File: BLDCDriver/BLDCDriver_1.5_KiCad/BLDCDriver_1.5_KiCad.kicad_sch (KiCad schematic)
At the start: 47 parts, among them IC1 STSPIN32G4, J1 Conn_01x02_Male, J2 Conn_01x07_Pin, J2 Motor Out, J4 POWER, J5 CAN, U3 MCP2562-E-SN, U5 AS5048A-HTSP-500, Y3 12Mhz

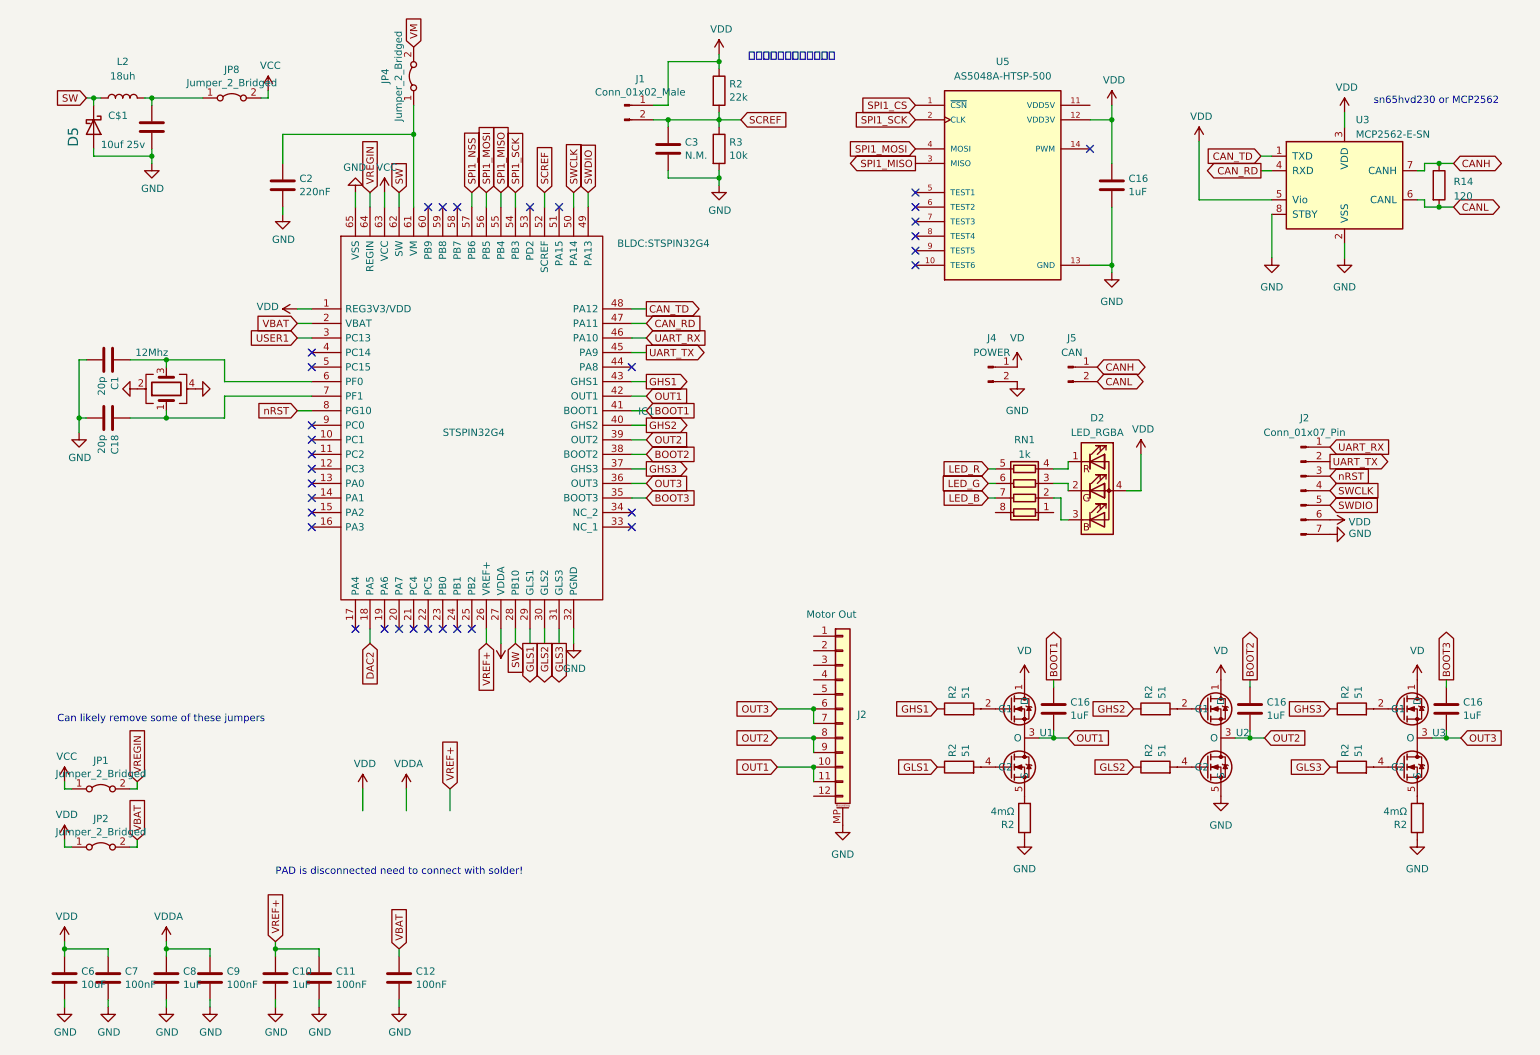
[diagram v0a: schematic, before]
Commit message: ✨回路を進めたよ。あとアートワーク太くするだけ。
CANの電源が3.3Vだと厳しい印象。
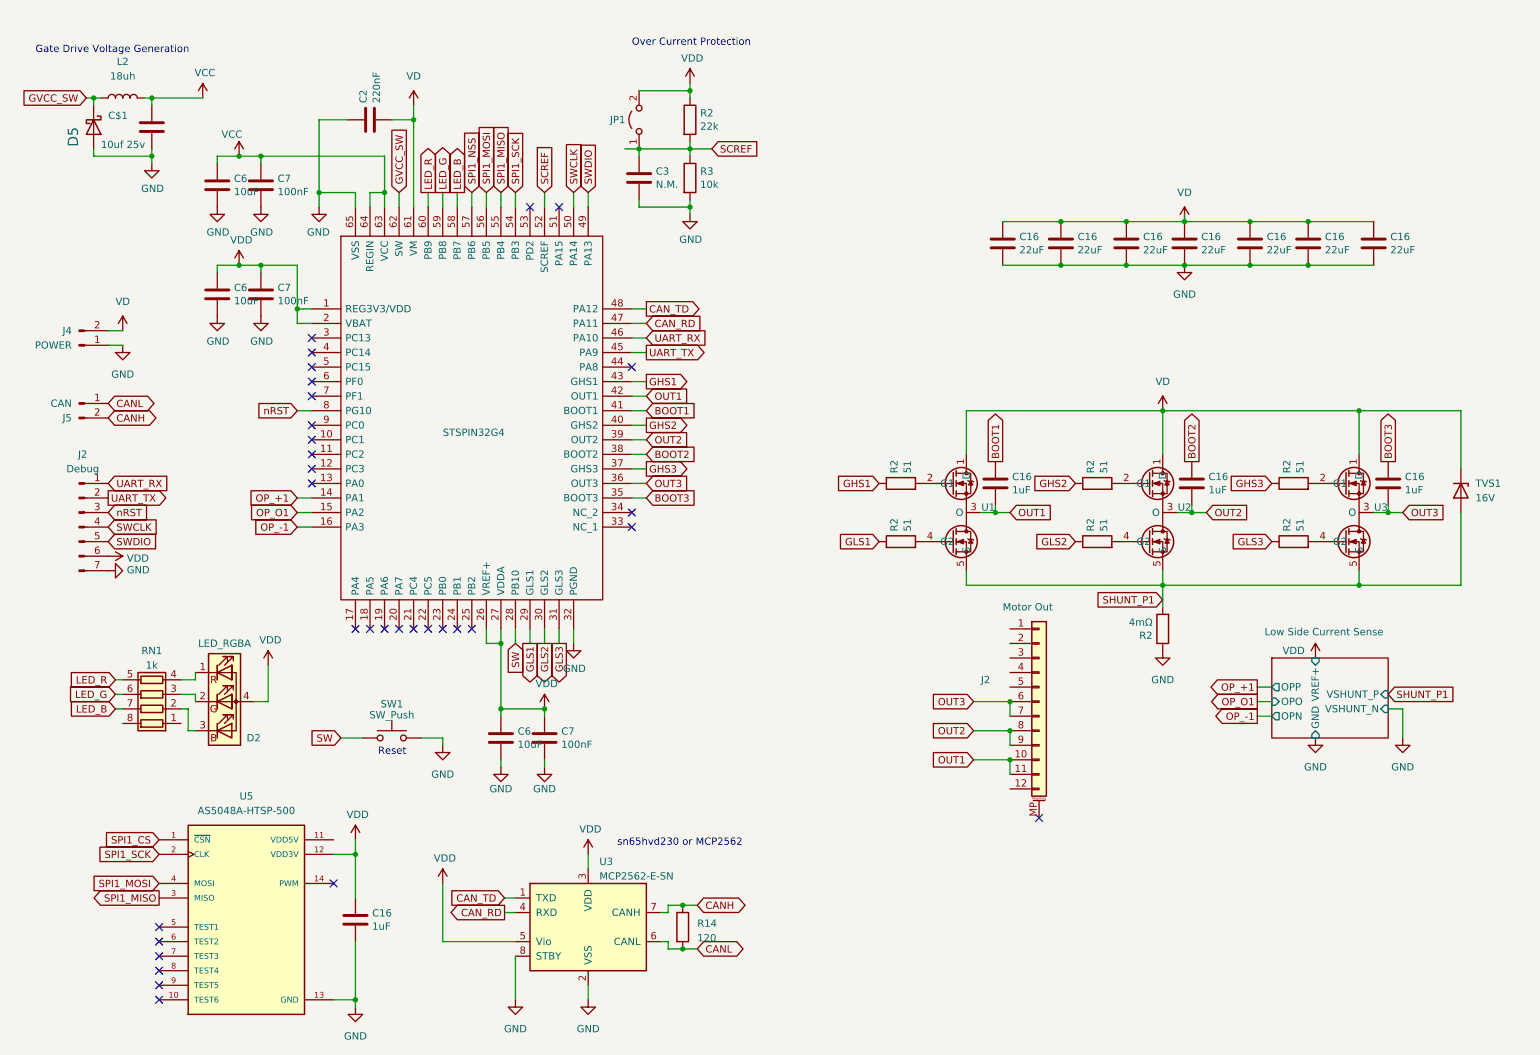
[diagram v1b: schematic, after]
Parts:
- removed C1, C18: 20p, Capacitor_SMD:C_0402_1005Metric, symbol Device:C
- removed C10, C8: 1uF, Capacitor_SMD:C_0603_1608Metric, symbol Device:C
- removed C11, C12, C7, C9: 100nF, Capacitor_SMD:C_0603_1608Metric, symbol Device:C
- removed C6: 10uF, Capacitor_SMD:C_0805_2012Metric, symbol Device:C
- removed J1: Conn_01x02_Male, Connector_PinSocket_2.54mm:PinSocket_1x02_P2.54mm_Vertical, symbol Connector:Conn_01x02_Male
- removed JP1, JP2, JP4, JP8: Jumper_2_Bridged, Jumper:SolderJumper-2_P1.3mm_Bridged_RoundedPad1.0x1.5mm, symbol Jumper:Jumper_2_Bridged
- removed R2 (x2): 4mΩ, Resistor_SMD:R_2512_6332Metric, symbol Device:R
- removed Y3: 12Mhz, Crystal:Crystal_SMD_3225-4Pin_3.2x2.5mm, symbol Device:Crystal_GND24
- added C16 (x7): 22uF, Capacitor_SMD:C_0805_2012Metric, symbol Device:C
- added C6 (x3): 10uF, Capacitor_SMD:C_0402_1005Metric, symbol Device:C
- added C7 (x3): 100nF, Capacitor_SMD:C_0402_1005Metric, symbol Device:C
- added JP1: Jumper_2_Open, Jumper:SolderJumper-2_P1.3mm_Open_RoundedPad1.0x1.5mm, symbol Jumper:Jumper_2_Open
- added R2: 4mΩ, Resistor_SMD:R_2512_6332Metric, symbol Device:R
- added SW1: SW_Push, newinov-kicad:SKRPACE010, symbol Switch:SW_Push
- added TVS1: 16V, Diode_SMD:D_SMB, symbol Device:D_Zener
- J2: value Conn_01x07_Pin -> Debug
- R14: footprint Resistor_SMD:R_0402_1005Metric_Pad0.72x0.64mm_HandSolder -> Resistor_SMD:R_0603_1608Metric_Pad0.98x0.95mm_HandSolder
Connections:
- net VBAT is gone; now on net VDD: IC1.2 (VBAT)
- net VDDA is gone; now on net VDD: IC1.27 (VDDA)
- net VREF+ is gone; now on net VDD: IC1.26 (VREF+)
- net VREGIN is gone; now on net VCC: IC1.64 (REGIN)
- net CANH: now also J5.2 (Pin_2); no longer J5.1 (Pin_1)
- net CANL: now also J5.1 (Pin_1); no longer J5.2 (Pin_2)
- net GND: now also C2.1, J4.1 (Pin_1), C16.1, C16.1, C16.1, C16.1, C16.1, C16.1, C16.1, C6.2, C6.2, C6.2, C7.2, C7.2, C7.2, R2.1, SW1.1; no longer C2.2, J2.MP (MountPin), J4.2 (Pin_2), U2.5 (S)
- net LED_B: now also IC1.58 (PB7)
- net LED_G: now also IC1.59 (PB8)
- net LED_R: now also IC1.60 (PB9)
- net SCREF: now also JP1.1 (A)
- net SW: now also SW1.2; no longer D5.1 (K), IC1.62 (SW), L2.1
- net VCC: now also C$1.1, L2.2, C6.1, C7.1
- net VD: now also C2.2, IC1.61 (VM), J4.2 (Pin_2), C16.2, C16.2, C16.2, C16.2, C16.2, C16.2, C16.2, TVS1.1 (K); no longer J4.1 (Pin_1)
- net VDD: now also C6.1, C6.1, C7.1, C7.1, JP1.2 (B)
- net SHUNT_P1: now reaches U3.5 (S)
- net SHUNT_P1: now also U1.5 (S), U2.5 (S), R2.2, TVS1.2 (A)
- net OP_+1: now reaches IC1.14 (PA1)
- net OP_O1: now reaches IC1.15 (PA2)
- net OP_-1: now reaches IC1.16 (PA3)
- net DAC2: no longer names the net of IC1.18 (PA5)
- net USER1: no longer names the net of IC1.3 (PC13)
- new net GVCC_SW: D5.1 (K), IC1.62 (SW), L2.1
- no-connect marks 33 -> 32
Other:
- added sheet Low Side Current Sense (CurrentSense.kicad_sch)
- note added: "Gate Drive Voltage Generation"
- note added: "Over Current Protection"
- note added: "Reset"
- note removed: "Can likely remove some of these jumpers"
- note removed: "PAD is disconnected need to connect with solder!"
- note removed: "入力電圧によって決定する"
- moved on the sheet: C16, C2, C3, D2, J2, J4, J5, R14, R2, R3, RN1, U1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

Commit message: ✨パワーラインのアートワークを仕上げた
[-] GNDビア
[-] CAN用LDO
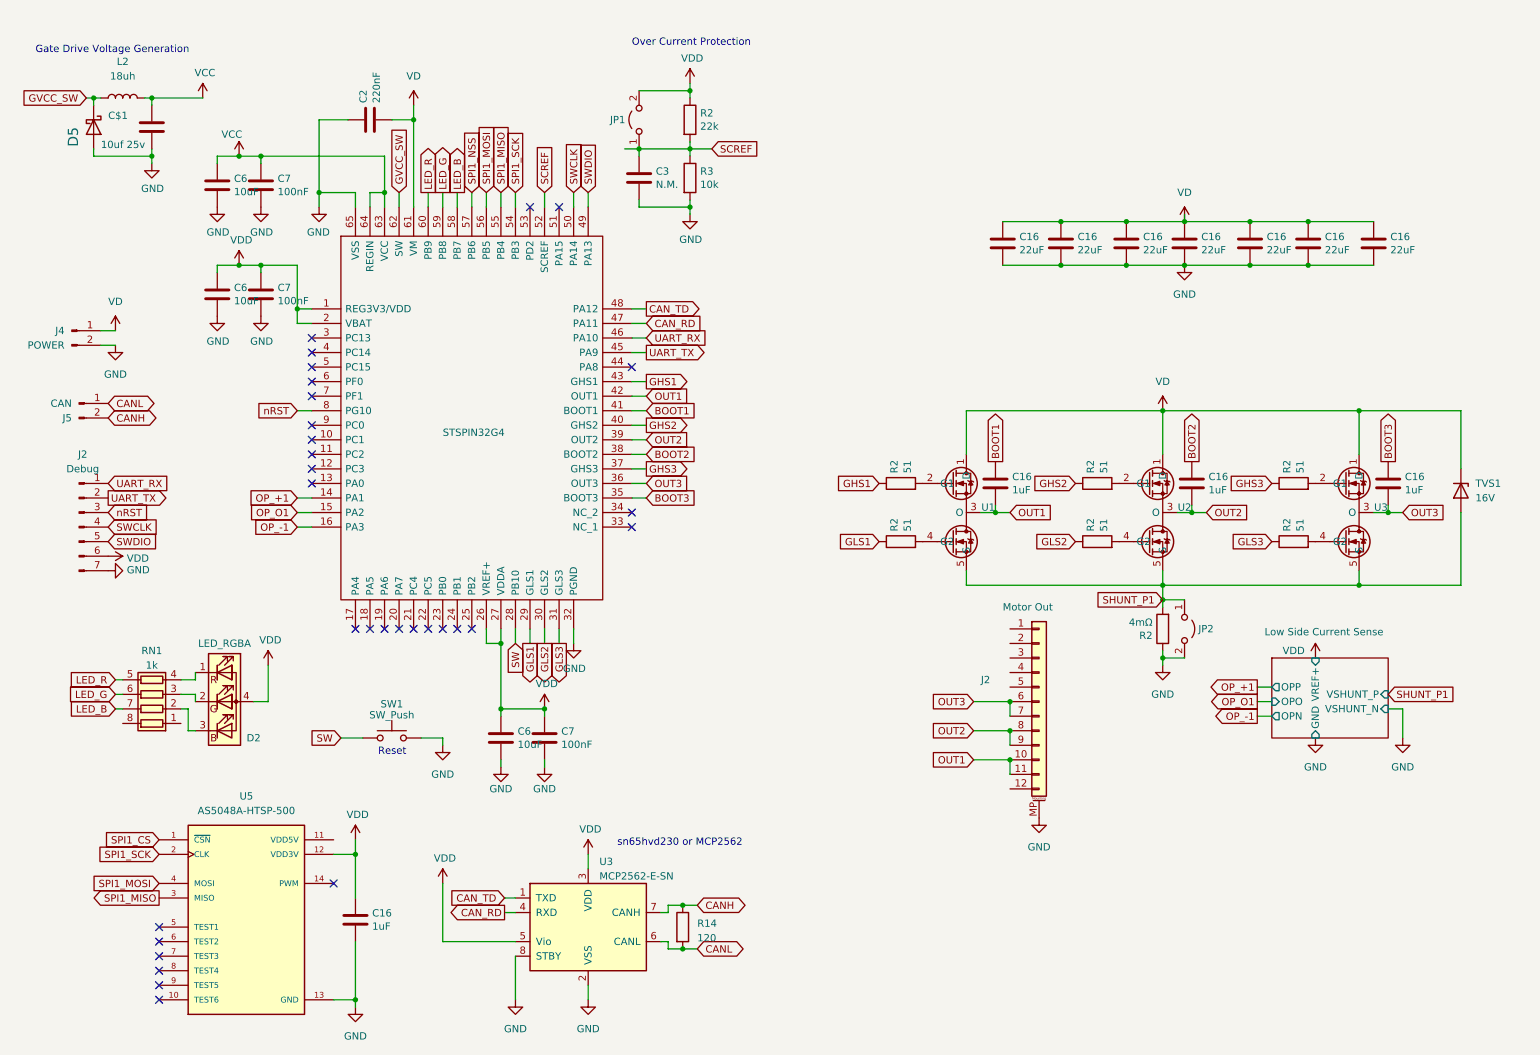
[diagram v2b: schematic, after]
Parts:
- added JP2: Jumper_2_Open, Jumper:SolderJumper-2_P1.3mm_Open_RoundedPad1.0x1.5mm, symbol Jumper:Jumper_2_Open
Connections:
- net GND: now also J2.MP (MountPin), J4.2 (Pin_2), JP2.2 (B); no longer J4.1 (Pin_1)
- net SHUNT_P1: now also JP2.1 (A)
- net VD: now also J4.1 (Pin_1); no longer J4.2 (Pin_2)
- no-connect marks 32 -> 31
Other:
- moved on the sheet: J4

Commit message: ✨ LED、LDO、ビアをやった
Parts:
- added C7 (x3): 100nF, Capacitor_SMD:C_0402_1005Metric, symbol Device:C
- added D3, D4, D5: LED, LED_SMD:LED_0603_1608Metric_Pad1.05x0.95mm_HandSolder, symbol Device:LED
- added R3 (x2): 1k, Resistor_SMD:R_0402_1005Metric, symbol Device:R
- added R3: 10k, Resistor_SMD:R_0402_1005Metric, symbol Device:R
- added U6: AP7375-33SA-7, AP7375-33SA-7_DIO, symbol BLDC_sym:AP7375-33SA-7
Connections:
- net GND: now also C7.2, C7.2, C7.2, D3.1 (K), D4.1 (K), D5.1 (K), U6.3 (GND)
- net VCC: now also C7.1, U6.1 (VIN)
- net VD: now also R3.1
- net VDD: now also R3.1; no longer U3.3 (VDD)
- net LED_Alive: now reaches IC1.53 (PD2)
- net LED_Alive: now also R3.1
- new net: D4.2 (A), R3.2
- new net: D3.2 (A), R3.2
- new net: D5.2 (A), R3.2
- new net +5V: C7.1, C7.1, U3.3 (VDD), U6.2 (VOUT)
- no-connect marks 31 -> 30

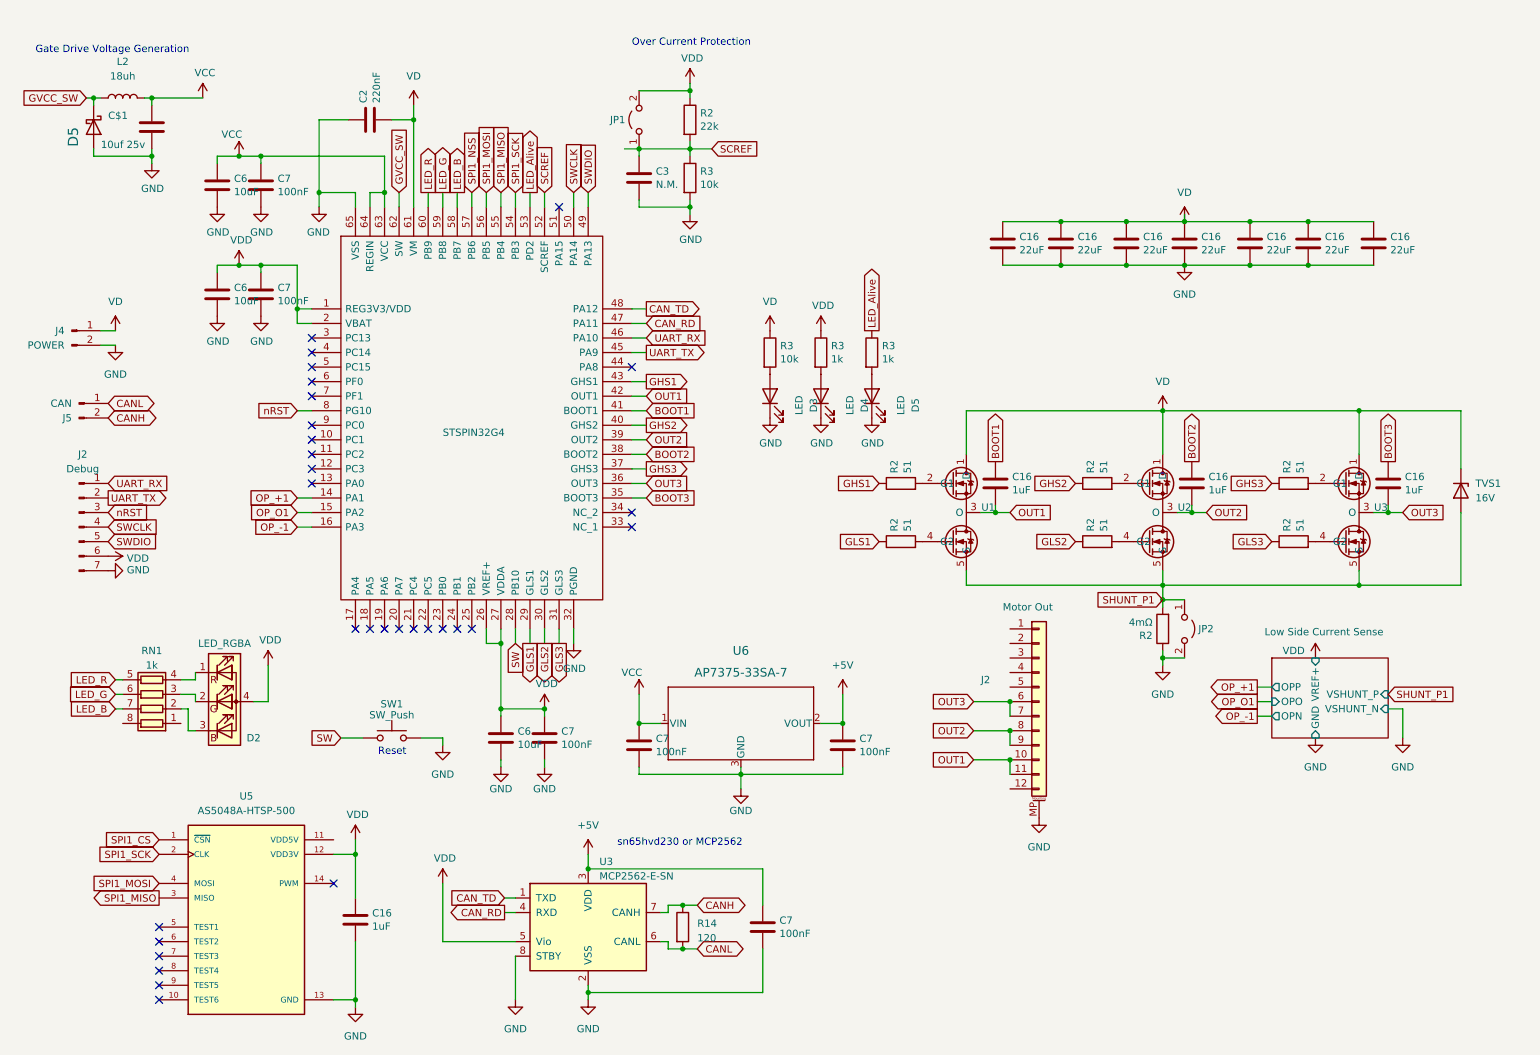
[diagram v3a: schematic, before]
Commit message: ✨ID切り替えパッド、GNDベタ、パターン禁止エリア設定、テストポイント
次は抵抗値の決定などをしていきたい。
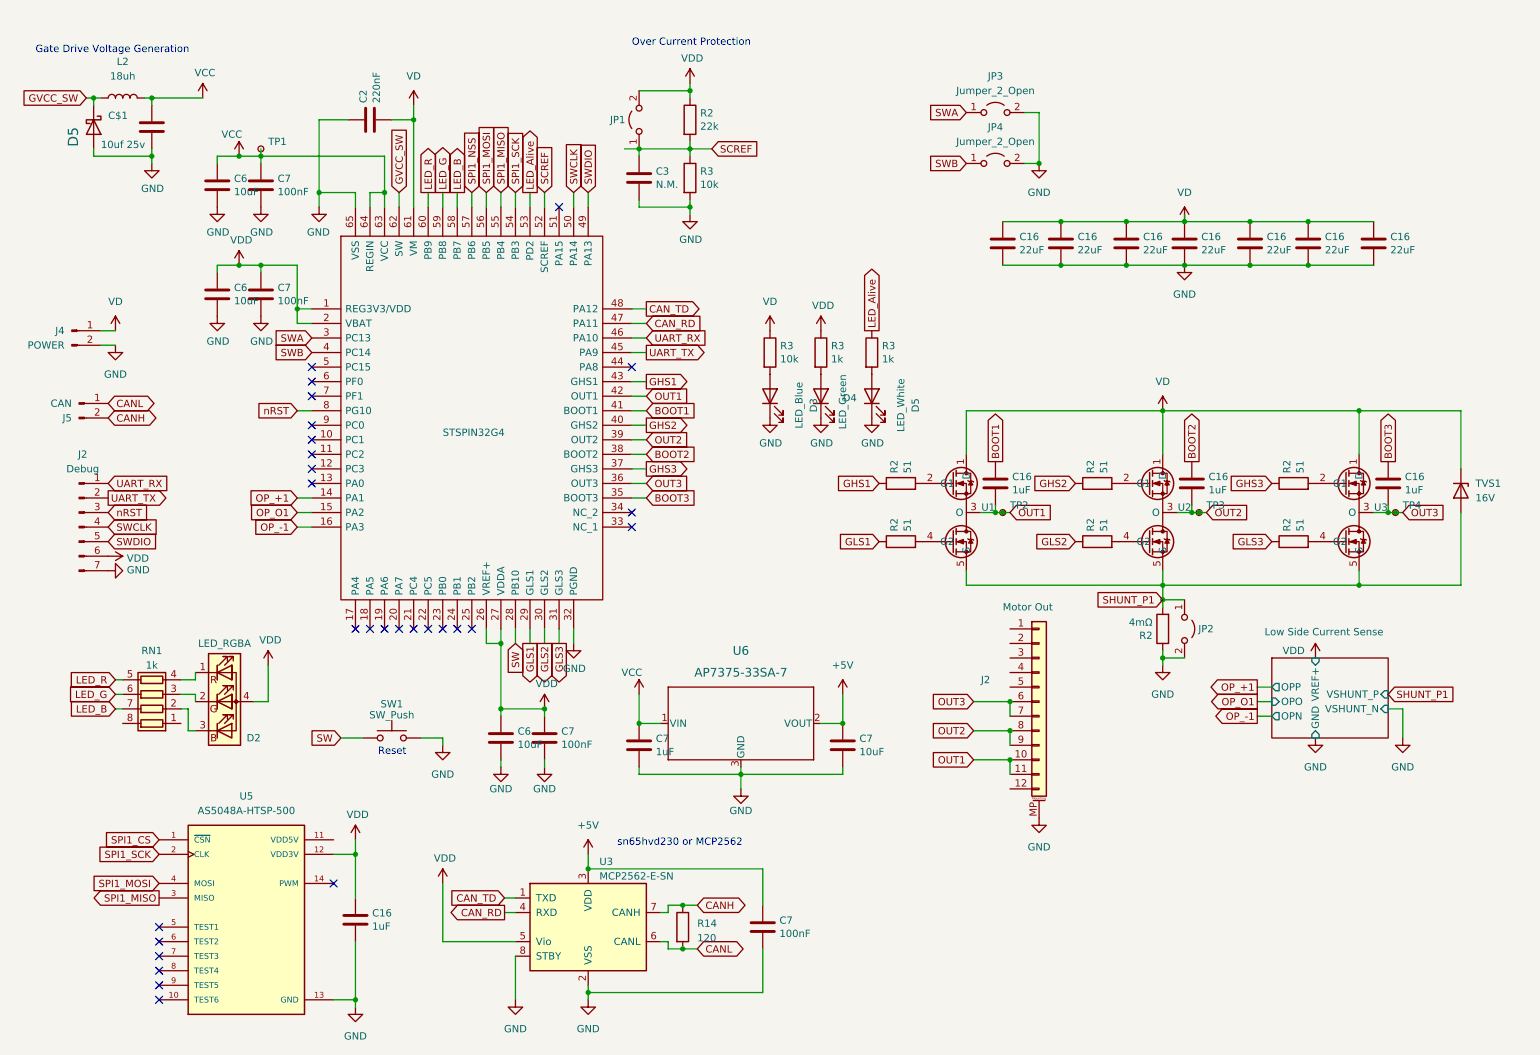
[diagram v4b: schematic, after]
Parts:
- added JP3, JP4: Jumper_2_Open, Jumper:SolderJumper-2_P1.3mm_Open_RoundedPad1.0x1.5mm, symbol Jumper:Jumper_2_Open
- added TP1, TP2, TP3, TP4: TestPoint_Small, TestPoint:TestPoint_Pad_D1.0mm, symbol Connector:TestPoint_Small
- C7: value 100nF -> 10uF
- C7: value 100nF -> 1uF
- D3: value LED -> LED_Blue
- D4: value LED -> LED_Green
- D5: value LED -> LED_White
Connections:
- net GND: now also JP3.2 (B), JP4.2 (B)
- net OUT1: now also TP2.1
- net OUT2: now also TP3.1
- net OUT3: now also TP4.1
- net VCC: now also TP1.1
- net SWA: now reaches IC1.3 (PC13)
- net SWA: now also JP3.1 (A)
- net SWB: now reaches IC1.4 (PC14)
- net SWB: now also JP4.1 (A)
- no-connect marks 30 -> 28
